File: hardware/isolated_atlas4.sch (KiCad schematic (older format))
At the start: 15 parts, among them J601 CONN_01X02, P6 ATLAS_ORP_PROBE, U601 ADM3260, U602 ATLAS_ORP

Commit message: Upgrade to Kicad 5.
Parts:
- C601, C602, C603, C604, C605, C606: symbol C -> fk-atlas-rescue:C
- J601: symbol CONN_01X02 -> fk-atlas-rescue:CONN_01X02
- P6: symbol WATER_PROBE -> fk-atlas-rescue:WATER_PROBE
- R601, R602, R603, R604, R605: symbol R -> fk-atlas-rescue:R
- U601: symbol adm3260 -> fk-atlas-rescue:adm3260
- U602: symbol ATLAS_SENSOR -> conservify:ATLAS_SENSOR
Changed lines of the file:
@@
-EESchema Schematic File Version 2
-LIBS:conservify
+EESchema Schematic File Version 4
 LIBS:fk-atlas-cache
-EELAYER 25 0
+EELAYER 26 0
 EELAYER END
 $Descr A4 11693 8268
@@
 $EndDescr
 $Comp
-L adm3260 U601
+L fk-atlas-rescue:adm3260 U601
 U 1 1 594C2CEF
 P 4400 2900
@@
 $EndComp
 $Comp
-L C C603
+L fk-atlas-rescue:C C603
 U 1 1 5948D4BD
 P 5650 3800
@@
 $EndComp
 $Comp
-L C C604
+L fk-atlas-rescue:C C604
 U 1 1 594C2CFA
 P 5650 4100
@@
 $EndComp
 $Comp
-L C C605
+L fk-atlas-rescue:C C605
 U 1 1 594C2CFD
 P 5650 4400
@@
 $EndComp
 $Comp
-L C C606
+L fk-atlas-rescue:C C606
 U 1 1 5948D5D0
 P 5650 4650
@@
 $EndComp
 $Comp
-L C C601
+L fk-atlas-rescue:C C601
 U 1 1 594C2D05
 P 2900 3800
@@
 $EndComp
 $Comp
-L C C602
+L fk-atlas-rescue:C C602
 U 1 1 594C2D0A
 P 2900 4100
@@
 $EndComp
 $Comp
-L R R601
+L fk-atlas-rescue:R R601
 U 1 1 5948D6B5
 P 5650 3300
@@
 $EndComp
 $Comp
-L R R602
+L fk-atlas-rescue:R R602
 U 1 1 5948E326
 P 6250 2700
@@
 $EndComp
 $Comp
-L R R604
+L fk-atlas-rescue:R R604
 U 1 1 594C2D13
 P 6700 2700
@@
 $EndComp
 $Comp
-L R R603
+L fk-atlas-rescue:R R603
 U 1 1 594C2D18
 P 6300 3250
@@
 $EndComp
 $Comp
-L R R605
+L fk-atlas-rescue:R R605
 U 1 1 594C2D1C
 P 6800 3250
@@
 $EndComp
 $Comp
-L VCC #PWR065
+L fk-atlas-rescue:VCC #PWR065
 U 1 1 594C2D25
 P 2450 3750
@@
 $EndComp
 $Comp
-L VCC #PWR066
+L fk-atlas-rescue:VCC #PWR066
 U 1 1 594C2D27
 P 2450 2350
@@
 $EndComp
 $Comp
-L ATLAS_SENSOR U602
+L conservify:ATLAS_SENSOR U602
 U 1 1 594C1D09
 P 8550 2900
@@
 $EndComp
 $Comp
-L CONN_01X02 J601
+L fk-atlas-rescue:CONN_01X02 J601
 U 1 1 59A1BC7E
 P 10200 2950
@@
 $EndComp
 $Comp
-L WATER_PROBE P6
+L fk-atlas-rescue:WATER_PROBE P6
 U 1 1 59D2AB5D
 P 8800 3600

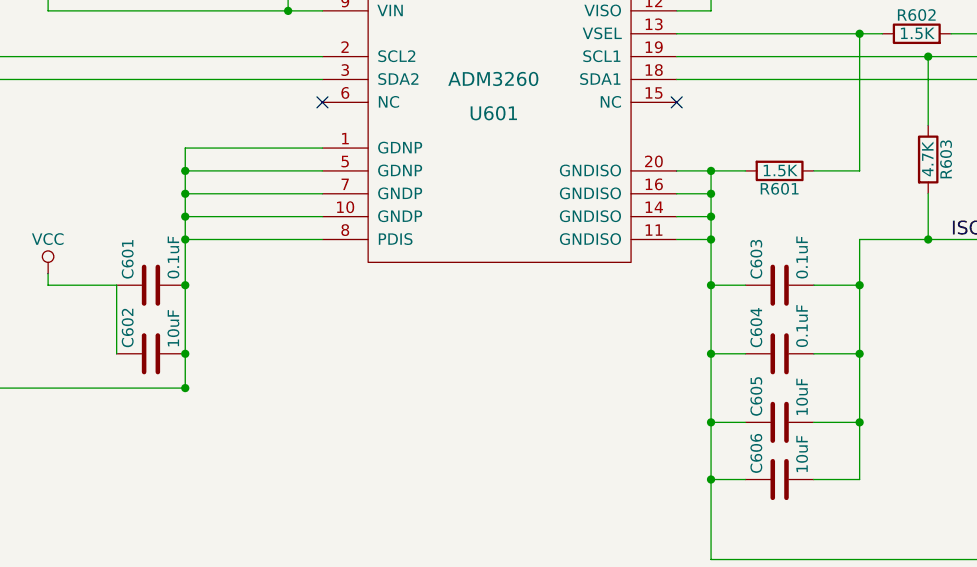
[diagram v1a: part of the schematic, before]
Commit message: Consistent part values across our schematics.
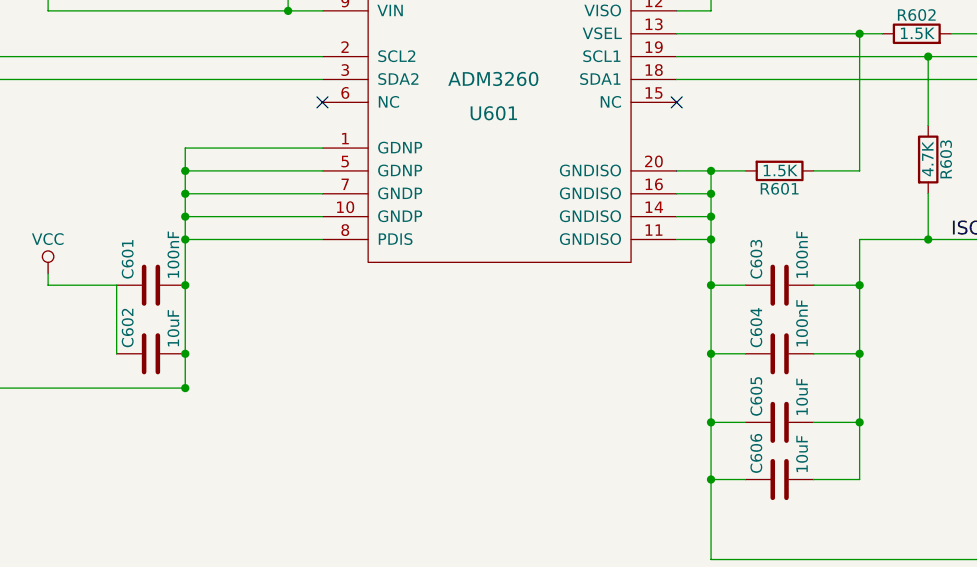
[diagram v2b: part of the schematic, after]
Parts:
- C601, C603, C604: value 0.1uF -> 100nF

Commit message: Part updates.
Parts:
- C601, C603, C604: Critical (none) -> (none); MFN (none) -> Murata Electronics; MFP (none) -> GRM188R71H104KA93D; Notes (none) -> (none); Package (none) -> (none); Source (none) -> ANY; Subsystem (none) -> (none); Supplier1 (none) -> mouser
- C602, C605, C606: Critical (none) -> (none); MFN (none) -> Taiyo Yuden; MFP (none) -> LMK107BBJ106KALT; Notes (none) -> (none); Package (none) -> (none); Source (none) -> ANY; Subsystem (none) -> (none); Supplier1 (none) -> mouser; spn1 81-GRM188R60J106ME47 -> 963-LMK107BBJ106KALT
- J601: Critical (none) -> (none); MFN (none) -> Amphenol RF; MFP (none) -> 031-5431; Notes (none) -> (none); Package (none) -> (none); Source (none) -> ANY; Subsystem (none) -> (none); Supplier1 (none) -> mouser
- P6: Critical (none) -> (none); MFN (none) -> (none); MFP (none) -> (none); Notes (none) -> (none); Package (none) -> (none); SPN1 (none) -> (none); Source (none) -> ANY; Subsystem (none) -> (none); Supplier1 (none) -> (none)
- R601, R602, R604: Critical (none) -> (none); MFN (none) -> (none); MFP (none) -> (none); Notes (none) -> (none); Package (none) -> (none); Source (none) -> ANY; Subsystem (none) -> (none); Supplier1 (none) -> (none)
- R603, R605: Critical (none) -> (none); MFN (none) -> Yageo; MFP (none) -> AF0603JR-074K7L; Notes (none) -> (none); Package (none) -> (none); Source (none) -> ANY; Subsystem (none) -> (none); Supplier1 (none) -> mouser
- U601: Critical (none) -> (none); MFN (none) -> Analog Devices / Linear Technology; MFP (none) -> ADM3260ARSZ; Notes (none) -> (none); Package (none) -> (none); Source (none) -> ANY; Subsystem (none) -> (none); Supplier1 (none) -> mouser
- U602: Critical (none) -> (none); MFN (none) -> (none); MFP (none) -> (none); Notes (none) -> (none); Package (none) -> (none); SPN1 (none) -> (none); Source (none) -> ANY; Subsystem (none) -> (none); Supplier1 (none) -> atlas

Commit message: Fix DRC in schematic mode.
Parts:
- C601, C602, C603, C604, C605, C606: symbol fk-atlas-rescue:C -> conservify:CAPACITOR_CERAMIC
- J601: symbol fk-atlas-rescue:CONN_01X02 -> conservify:CONN_01x02
- P6: symbol fk-atlas-rescue:WATER_PROBE -> conservify:ATLAS_WATER_PROBE
- R601, R602, R603, R604, R605: symbol fk-atlas-rescue:R -> conservify:R
- U601: symbol fk-atlas-rescue:adm3260 -> conservify:ADM3260
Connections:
- wire segments 52 -> 78
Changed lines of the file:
@@
 $EndDescr
 $Comp
-L fk-atlas-rescue:adm3260 U601
+L conservify:ADM3260 U601
 U 1 1 594C2CEF
 P 4400 2900
@@
 $EndComp
 $Comp
-L fk-atlas-rescue:C C603
+L conservify:CAPACITOR_CERAMIC C603
 U 1 1 5948D4BD
 P 5650 3800
@@
 $EndComp
 $Comp
-L fk-atlas-rescue:C C604
+L conservify:CAPACITOR_CERAMIC C604
 U 1 1 594C2CFA
 P 5650 4100
@@
 $EndComp
 $Comp
-L fk-atlas-rescue:C C605
+L conservify:CAPACITOR_CERAMIC C605
 U 1 1 594C2CFD
 P 5650 4400
@@
 $EndComp
 $Comp
-L fk-atlas-rescue:C C606
+L conservify:CAPACITOR_CERAMIC C606
 U 1 1 5948D5D0
 P 5650 4650
@@
 $EndComp
 $Comp
-L fk-atlas-rescue:C C601
+L conservify:CAPACITOR_CERAMIC C601
 U 1 1 594C2D05
 P 2900 3800
@@
 $EndComp
 $Comp
-L fk-atlas-rescue:C C602
+L conservify:CAPACITOR_CERAMIC C602
 U 1 1 594C2D0A
 P 2900 4100
@@
 $EndComp
 $Comp
-L fk-atlas-rescue:R R601
+L conservify:R R601
 U 1 1 5948D6B5
 P 5650 3300
@@
 $EndComp
 $Comp
-L fk-atlas-rescue:R R602
+L conservify:R R602
 U 1 1 5948E326
 P 6250 2700
@@
 $EndComp
 $Comp
-L fk-atlas-rescue:R R604
+L conservify:R R604
 U 1 1 594C2D13
 P 6700 2700
@@
 $EndComp
 $Comp
-L fk-atlas-rescue:R R603
+L conservify:R R603
 U 1 1 594C2D18
 P 6300 3250
@@
 $EndComp
 $Comp
-L fk-atlas-rescue:R R605
+L conservify:R R605
 U 1 1 594C2D1C
 P 6800 3250
@@
 $EndComp
 $Comp
-L fk-atlas-rescue:VCC #PWR065
+L conservify:VCC #PWR065
 U 1 1 594C2D25
 P 2450 3750
@@
 $EndComp
 $Comp
-L fk-atlas-rescue:VCC #PWR066
+L conservify:VCC #PWR066
 U 1 1 594C2D27
 P 2450 2350
@@
 $EndComp
 $Comp
-L fk-atlas-rescue:CONN_01X02 J601
+L conservify:CONN_01x02 J601
 U 1 1 59A1BC7E
-P 10200 2950
-F 0 "J601" H 10200 3100 50  0000 C CNN
-F 1 "CONN_01X02" V 10300 2950 50  0000 C CNN
-F 2 "conservify:BNC" H 10200 2950 50  0001 C CNN
-F 3 "" H 10200 2950 50  0001 C CNN
-F 4 " " H 10200 3200 50  0001 C CNN "Critical"
-F 5 "Amphenol RF" H 10200 3200 50  0001 C CNN "MFN"
-F 6 "031-5431" H 10200 3200 50  0001 C CNN "MFP"
-F 7 " " H 10200 3200 50  0001 C CNN "Notes"
-F 8 " " H 10200 3200 50  0001 C CNN "Package"
-F 9 "ANY" H 10200 3200 50  0001 C CNN "Source"
-F 10 " " H 10200 3200 50  0001 C CNN "Subsystem"
-F 11 "mouser" H 10200 3200 50  0001 C CNN "Supplier1"
-F 12 "0" H 10200 3200 50  0001 C CNN "price"
-F 13 "523-31-5431" H 350 0   50  0001 C CNN "spn1"
-	1    10200 2950
-	1    0    0    -1
-$EndComp
-$Comp
-L fk-atlas-rescue:WATER_PROBE P6
+P 10200 2900
+F 0 "J601" H 10200 3050 50  0000 C CNN
+F 1 "CONN_01X02" V 10300 2900 50  0000 C CNN
+F 2 "conservify:BNC" H 10200 2900 50  0001 C CNN
+F 3 "" H 10200 2900 50  0001 C CNN
+F 4 " " H 10200 3150 50  0001 C CNN "Critical"
+F 5 "Amphenol RF" H 10200 3150 50  0001 C CNN "MFN"
+F 6 "031-5431" H 10200 3150 50  0001 C CNN "MFP"
+F 7 " " H 10200 3150 50  0001 C CNN "Notes"
+F 8 " " H 10200 3150 50  0001 C CNN "Package"
+F 9 "ANY" H 10200 3150 50  0001 C CNN "Source"
+F 10 " " H 10200 3150 50  0001 C CNN "Subsystem"
+F 11 "mouser" H 10200 3150 50  0001 C CNN "Supplier1"
+F 12 "0" H 10200 3150 50  0001 C CNN "price"
+F 13 "523-31-5431" H 350 -50 50  0001 C CNN "spn1"
+	1    10200 2900
+	1    0    0    -1
+$EndComp
+$Comp
+L conservify:ATLAS_WATER_PROBE P6
 U 1 1 59D2AB5D
 P 8800 3600
@@
 F 12 " " H 8800 3700 50  0001 C CNN "Supplier1"
 	1    8800 3600
+	1    0    0    -1
+$EndComp
+$Comp
+L conservify:PWR_FLAG #FLG0109
+U 1 1 5BCDD0A6
+P 7400 4900
+F 0 "#FLG0109" H 7400 4975 50  0001 C CNN
+F 1 "PWR_FLAG" H 7400 5050 50  0000 C CNN
+F 2 "" H 7400 4900 50  0001 C CNN
+F 3 "~" H 7400 4900 50  0001 C CNN
+	1    7400 4900
 	1    0    0    -1
 $EndComp
@@
 ORP_PGND
 Wire Wire Line
-	5200 3300 5500 3300
-Wire Wire Line
-	5350 3300 5350 5000
+	5200 3300 5350 3300
+Wire Wire Line
+	5350 3300 5350 3400
 Wire Wire Line
 	5350 3600 5200 3600
@@
 	5800 3800 6000 3800
 Wire Wire Line
-	6000 3600 6000 4650
+	6000 3600 6000 3800
 Wire Wire Line
 	6000 4650 5800 4650
@@
 	5800 4100 6000 4100
 Wire Wire Line
-	5200 2800 7800 2800
-Wire Wire Line
-	5200 2900 7800 2900
-Wire Wire Line
-	5200 2700 6100 2700
+	5200 2800 6300 2800
+Wire Wire Line
+	5200 2900 6800 2900
+Wire Wire Line
+	5200 2700 6000 2700
 Wire Wire Line
 	6000 2700 6000 3300
@@
 	5350 2600 5350 2500
 Wire Wire Line
-	5200 2500 7400 2500
+	5200 2500 5350 2500
 Wire Wire Line
 	6900 2500 6900 2700
@@
 	6300 3400 6300 3600
 Wire Wire Line
-	6000 3600 6800 3600
+	6000 3600 6300 3600
 Wire Wire Line
 	6800 3600 6800 3400
 Wire Wire Line
-	2450 2600 3650 2600
-Wire Wire Line
-	2450 2350 2450 2600
+	2450 2600 3500 2600
+Wire Wire Line
+	2450 2350 2450 2450
 Wire Wire Line
 	3650 2500 3500 2500
@@
 	9450 3000 10000 3000
 Wire Wire Line
-	3050 3200 3050 4250
+	3050 3200 3050 3300
+Wire Wire Line
+	5350 3500 5350 3600
+Wire Wire Line
+	5350 3400 5350 3500
+Wire Wire Line
+	5350 3600 5350 3800
+Wire Wire Line
+	5350 4400 5350 4650
+Wire Wire Line
+	5350 4100 5350 4400
+Wire Wire Line
+	5350 3800 5350 4100
+Wire Wire Line
+	6000 4400 6000 4650
+Wire Wire Line
+	6000 4100 6000 4400
+Wire Wire Line
+	5350 3300 5500 3300
+Wire Wire Line
+	5350 2500 6900 2500
+Wire Wire Line
+	6000 2700 6100 2700
+Wire Wire Line
+	6300 2800 7800 2800
+Wire Wire Line
+	6800 2900 7800 2900
+Wire Wire Line
+	3500 2600 3650 2600
+Wire Wire Line
+	3050 3800 3050 4100
+Wire Wire Line
+	3050 4100 3050 4250
+Wire Wire Line
+	3050 3600 3050 3800
+Wire Wire Line
+	3050 3500 3050 3600
+Wire Wire Line
+	3050 3400 3050 3500
+Wire Wire Line
+	3050 3300 3050 3400
+Wire Wire Line
+	2450 2450 2450 2600
+Wire Wire Line
+	5350 4650 5350 5000
+Wire Wire Line
+	6300 3600 6800 3600
+Wire Wire Line
+	6000 3800 6000 4100
+Wire Wire Line
+	6900 2500 7400 2500
+Wire Wire Line
+	7400 4900 7400 5000
 Connection ~ 5350 3500
 Connection ~ 5350 3400
@@
 Connection ~ 6300 3600
 Connection ~ 6000 3800
-Connection ~ 3050 4250
 Connection ~ 6900 2500
 NoConn ~ 3650 3000

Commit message: Drop prototype Atlas modules - focus on getting OEM boards working.
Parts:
- U602: footprint conservify:ATLAS_SENSOR_BOARD_COMBO -> conservify:ATLAS_SENSOR_BOARD_OEM
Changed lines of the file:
@@
 F 0 "U602" H 8100 2550 60  0000 C CNN
 F 1 "ATLAS_ORP" H 8600 2850 60  0000 C CNN
-F 2 "conservify:ATLAS_SENSOR_BOARD_COMBO" H 8550 2900 60  0001 C CNN
+F 2 "conservify:ATLAS_SENSOR_BOARD_OEM" H 8550 2900 60  0001 C CNN
 F 3 "" H 8550 2900 60  0001 C CNN
 F 4 " " H 8100 2650 50  0001 C CNN "Critical"
